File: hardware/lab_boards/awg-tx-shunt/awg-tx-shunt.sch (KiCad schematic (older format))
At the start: 20 parts, among them J1 1-1337543-0, J2 1-1337543-0, J3 1-1337543-0, J4 1-1337543-0, J5 1-1337543-0

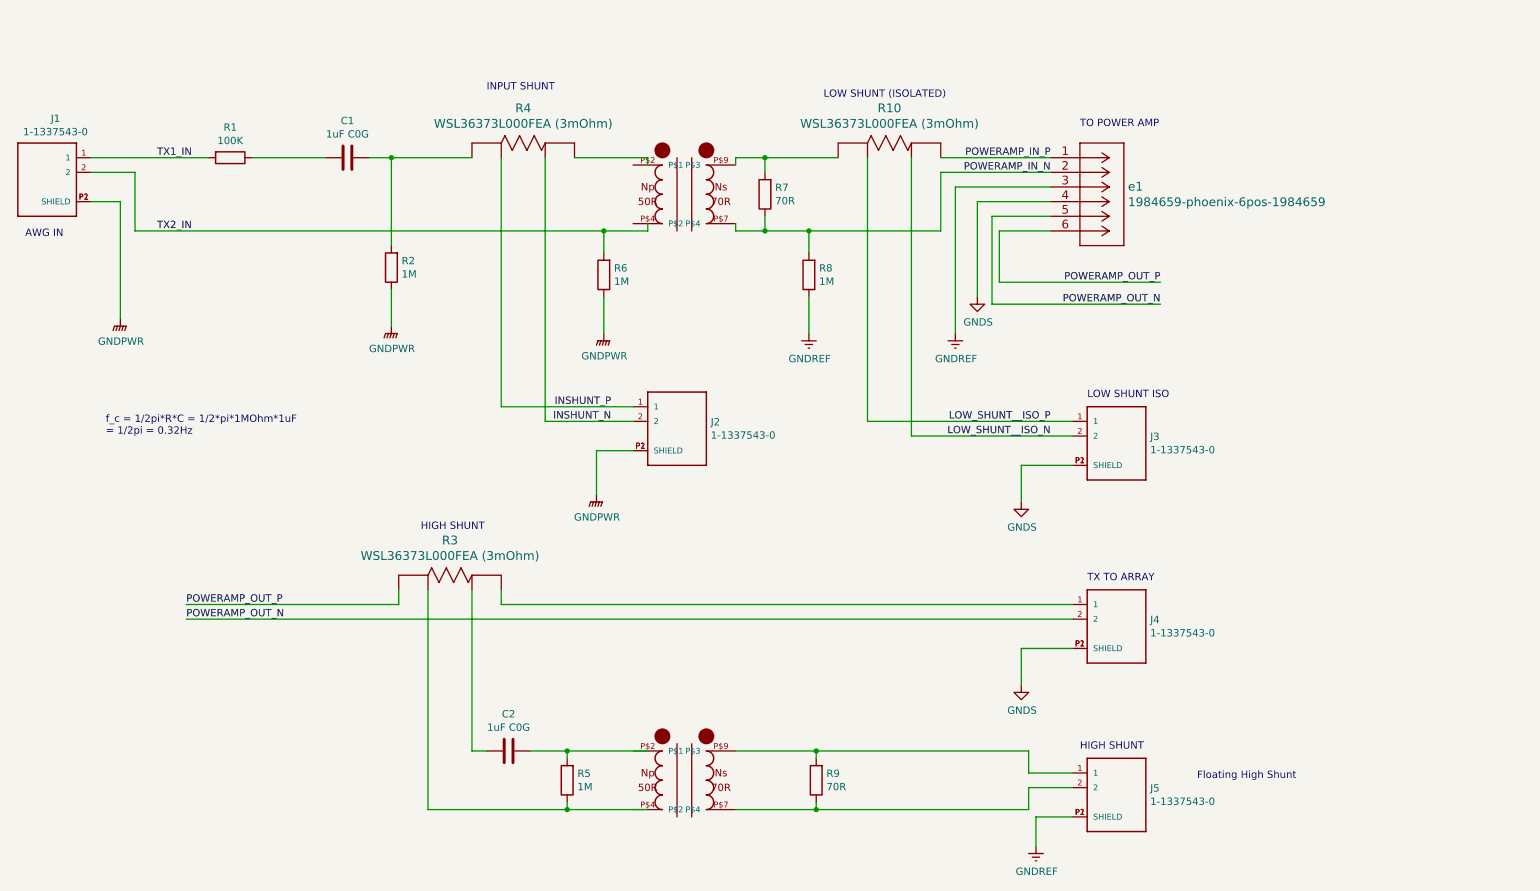
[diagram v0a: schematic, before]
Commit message: reworked the whole board so the grounds are properly isolated and can be connected to a common star ground offboard. No vias are necessary for routing, either, which is a good thing for signal integrity.
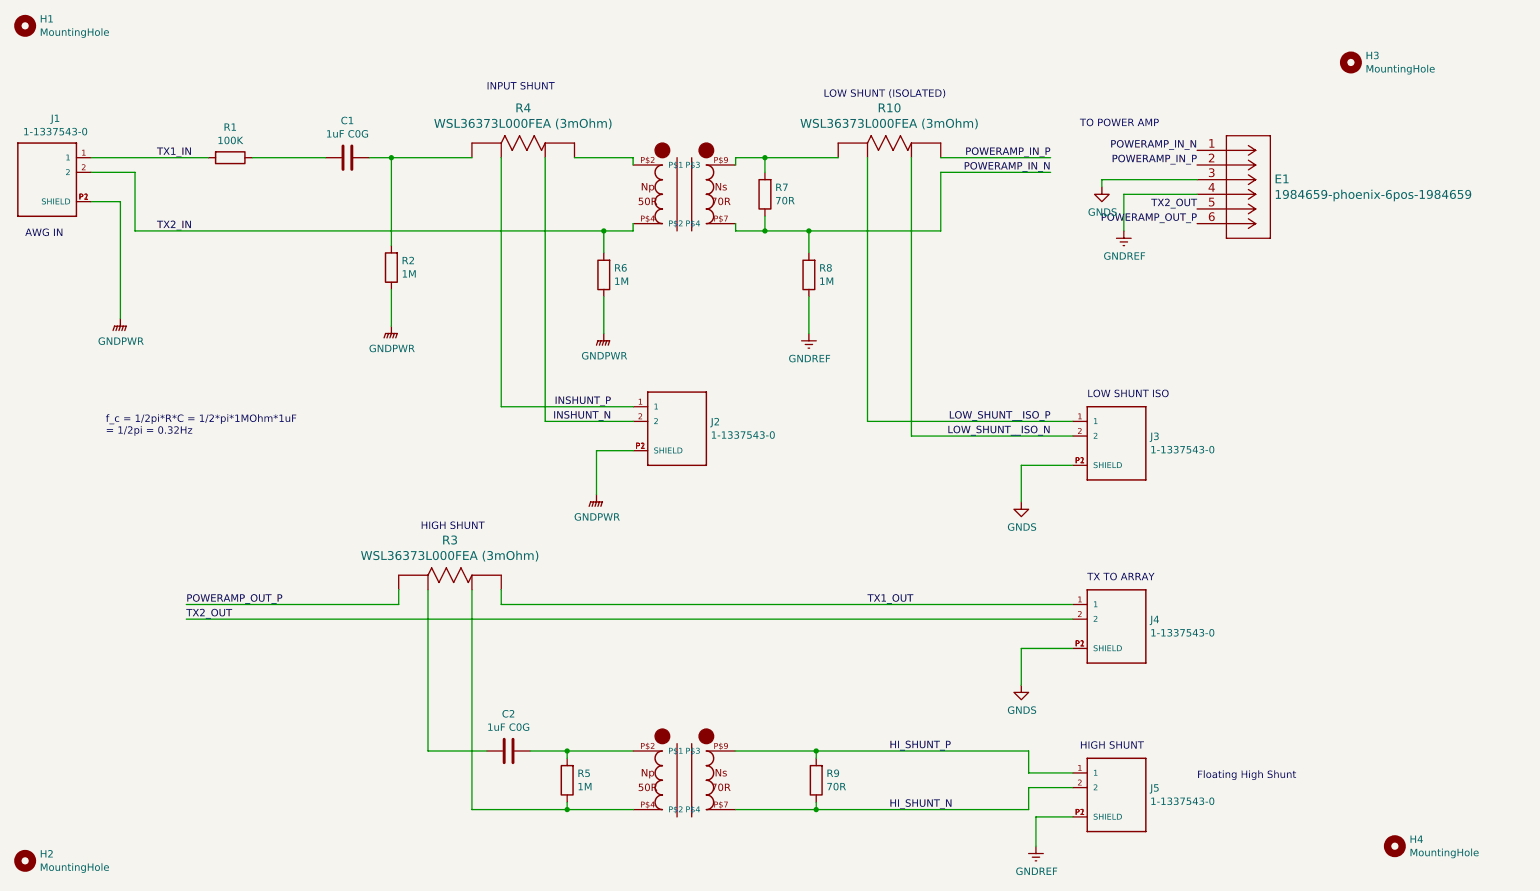
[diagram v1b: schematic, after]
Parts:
- added H1, H2, H3, H4: MountingHole, MountingHole:MountingHole_3.2mm_M3_Pad_Via, symbol Mechanical:MountingHole
- E1: renamed from e1; footprint CONN_1984659_PXC -> phoenix-6pos-1984659:1984659
- R10, R3, R4: footprint WSL3637_VIS -> WSL36373L000FEA:WSL36373L000FEA
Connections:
- net labels added: HI_SHUNT_N, HI_SHUNT_P, TX1_OUT, TX2_OUT
- net labels removed: POWERAMP_OUT_N
- wire segments 81 -> 75
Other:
- moved on the sheet: E1
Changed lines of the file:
@@
 F 0 "R4" H 4200 1988 60  0000 C CNN
 F 1 "WSL36373L000FEA (3mOhm)" H 4200 1882 60  0000 C CNN
-F 2 "WSL3637_VIS" H 4200 1315 60  0001 C CNN
+F 2 "WSL36373L000FEA:WSL36373L000FEA" H 4200 1315 60  0001 C CNN
 F 3 "" H 3950 1650 60  0000 C CNN
 	1    3950 1650
@@
 	3300 2550 3300 2800
 Wire Wire Line
-	4550 1650 5050 1650
-Wire Wire Line
-	5050 1650 5050 1700
-Wire Wire Line
-	5050 2100 5050 2150
+	4550 1650 4950 1650
 $Comp
 L Device:R R6
@@
 Wire Wire Line
 	4750 2300 4750 2150
-Connection ~ 4750 2150
-Wire Wire Line
-	4750 2150 5050 2150
 Wire Wire Line
 	4750 2600 4750 2850
@@
 F 0 "R3" H 3700 4938 60  0000 C CNN
 F 1 "WSL36373L000FEA (3mOhm)" H 3700 4832 60  0000 C CNN
-F 2 "WSL3637_VIS" H 3700 4265 60  0001 C CNN
+F 2 "WSL36373L000FEA:WSL36373L000FEA" H 3700 4265 60  0001 C CNN
 F 3 "" H 3450 4600 60  0000 C CNN
 	1    3450 4600
@@
 F 0 "R10" H 6700 1988 60  0000 C CNN
 F 1 "WSL36373L000FEA (3mOhm)" H 6700 1882 60  0000 C CNN
-F 2 "WSL3637_VIS" H 6700 1315 60  0001 C CNN
+F 2 "WSL36373L000FEA:WSL36373L000FEA" H 6700 1315 60  0001 C CNN
 F 3 "" H 6450 1650 60  0000 C CNN
 	1    6450 1650
@@
 	7050 1750 7050 2150
 Wire Wire Line
-	7800 1850 7150 1850
-Wire Wire Line
-	7800 1950 7300 1950
+	8800 1900 8300 1900
 Wire Wire Line
 	1250 1650 2050 1650
@@
 	1    0    0    -1
 $EndComp
-Wire Wire Line
-	7300 1950 7300 2600
-Wire Wire Line
-	7150 1850 7150 2850
 $Comp
 L Device:R R8
@@
 	4050 4700 7950 4700
 Wire Wire Line
-	3850 4600 3850 5700
-Wire Wire Line
-	3850 5700 3950 5700
-Wire Wire Line
-	5050 6100 4500 6100
-Wire Wire Line
-	3550 6100 3550 4600
-Wire Wire Line
 	1900 4800 7950 4800
 Wire Wire Line
@@
 TO POWER AMP
 $Comp
-L awg-tx-shunt-rescue:1984659-phoenix-6pos-1984659 e1
+L awg-tx-shunt-rescue:1984659-phoenix-6pos-1984659 E1
 U 1 1 5F8227D9
-P 7800 1650
-F 0 "e1" H 8328 1453 60  0000 L CNN
-F 1 "1984659-phoenix-6pos-1984659" H 8328 1347 60  0000 L CNN
-F 2 "CONN_1984659_PXC" H 8200 1390 60  0001 C CNN
-F 3 "" H 7800 1650 60  0000 C CNN
-	1    7800 1650
+P 8800 1600
+F 0 "E1" H 9328 1403 60  0000 L CNN
+F 1 "1984659-phoenix-6pos-1984659" H 9328 1297 60  0000 L CNN
+F 2 "phoenix-6pos-1984659:1984659" H 9200 1340 60  0001 C CNN
+F 3 "" H 8800 1600 60  0000 C CNN
+	1    8800 1600
 	1    0    0    -1
 $EndComp
@@
 Wire Wire Line
 	7600 3750 7600 4000
-Wire Wire Line
-	7800 2050 7400 2050
-Wire Wire Line
-	7400 2050 7400 2650
-Wire Wire Line
-	7400 2650 8550 2650
-Wire Wire Line
-	7800 2150 7450 2150
-Wire Wire Line
-	7450 2150 7450 2500
-Wire Wire Line
-	7450 2500 8550 2500
 $Comp
 L Conn-BNC-Amphenol-Isolated-1-1337543-0:1-1337543-0 J2
@@
 Wire Wire Line
 	6150 2150 7050 2150
-Text Label 8550 2500 2    50   ~ 0
-POWERAMP_OUT_P
-Text Label 8550 2650 2    50   ~ 0
-POWERAMP_OUT_N
 Wire Wire Line
 	4500 5700 4500 5750
-Connection ~ 4500 5700
-Wire Wire Line
-	4500 5700 5050 5700
 Wire Wire Line
 	4500 6050 4500 6100
-Connection ~ 4500 6100
-Wire Wire Line
-	4500 6100 3550 6100
+Wire Wire Line
+	4500 6100 3850 6100
 Wire Wire Line
 	7950 5000 7600 5000
@@
 Text Label 1900 4700 0    50   ~ 0
 POWERAMP_OUT_P
-Text Label 1900 4800 0    50   ~ 0
-POWERAMP_OUT_N
 Wire Wire Line
 	7950 6150 7700 6150
@@
 $EndComp
 $Comp
+L power:GNDREF #PWR0110
+U 1 1 5F8F2A85
+P 8300 2150
+F 0 "#PWR0110" H 8300 1900 50  0001 C CNN
+F 1 "GNDREF" H 8305 1977 50  0000 C CNN
+F 2 "" H 8300 2150 50  0001 C CNN
+F 3 "" H 8300 2150 50  0001 C CNN
+	1    8300 2150
+	1    0    0    -1
+$EndComp
+Text Label 6700 5700 0    50   ~ 0
+HI_SHUNT_P
+Text Label 6700 6100 0    50   ~ 0
+HI_SHUNT_N
+Text Label 6550 4700 0    50   ~ 0
+TX1_OUT
+Text Label 1900 4800 0    50   ~ 0
+TX2_OUT
+Wire Wire Line
+	4950 1650 4950 1700
+Wire Wire Line
+	4950 2100 4950 2150
+Wire Wire Line
+	4950 2150 4750 2150
+Connection ~ 4750 2150
+Wire Wire Line
+	4950 5700 4500 5700
+Connection ~ 4500 5700
+Wire Wire Line
+	4950 6100 4500 6100
+Connection ~ 4500 6100
+Wire Wire Line
+	3550 5700 3550 4600
+Wire Wire Line
+	3850 4600 3850 6100
+Wire Wire Line
+	3950 5700 3550 5700
+Text Label 8800 1600 2    50   ~ 0
+POWERAMP_IN_N
+Text Label 8800 1700 2    50   ~ 0
+POWERAMP_IN_P
+Text Label 8800 2100 2    50   ~ 0
+POWERAMP_OUT_P
+Text Label 8800 2000 2    50   ~ 0
+TX2_OUT
+$Comp
 L power:GNDS #PWR0109
 U 1 1 5F8EF65F
-P 7300 2600
-F 0 "#PWR0109" H 7300 2350 50  0001 C CNN
-F 1 "GNDS" H 7305 2427 50  0000 C CNN
-F 2 "" H 7300 2600 50  0001 C CNN
-F 3 "" H 7300 2600 50  0001 C CNN
-	1    7300 2600
-	1    0    0    -1
-$EndComp
-$Comp
-L power:GNDREF #PWR0110
-U 1 1 5F8F2A85
-P 7150 2850
-F 0 "#PWR0110" H 7150 2600 50  0001 C CNN
-F 1 "GNDREF" H 7155 2677 50  0000 C CNN
-F 2 "" H 7150 2850 50  0001 C CNN
-F 3 "" H 7150 2850 50  0001 C CNN
-	1    7150 2850
-	1    0    0    -1
-$EndComp
+P 8150 1850
+F 0 "#PWR0109" H 8150 1600 50  0001 C CNN
+F 1 "GNDS" H 8155 1677 50  0000 C CNN
+F 2 "" H 8150 1850 50  0001 C CNN
+F 3 "" H 8150 1850 50  0001 C CNN
+	1    8150 1850
+	1    0    0    -1
+$EndComp
+Wire Wire Line
+	8300 1900 8300 2150
+$Comp
+L Mechanical:MountingHole H3
+U 1 1 5F9CEF90
+P 9850 1000
+F 0 "H3" H 9950 1046 50  0000 L CNN
+F 1 "MountingHole" H 9950 955 50  0000 L CNN
+F 2 "MountingHole:MountingHole_3.2mm_M3_Pad_Via" H 9850 1000 50  0001 C CNN
+F 3 "~" H 9850 1000 50  0001 C CNN
+	1    9850 1000
+	1    0    0    -1
+$EndComp
+$Comp
+L Mechanical:MountingHole H4
+U 1 1 5F9CF560
+P 10150 6350
+F 0 "H4" H 10250 6396 50  0000 L CNN
+F 1 "MountingHole" H 10250 6305 50  0000 L CNN
+F 2 "MountingHole:MountingHole_3.2mm_M3_Pad_Via" H 10150 6350 50  0001 C CNN
+F 3 "~" H 10150 6350 50  0001 C CNN
+	1    10150 6350
+	1    0    0    -1
+$EndComp
+$Comp
+L Mechanical:MountingHole H2
+U 1 1 5F9D0AA7
+P 800 6450
+F 0 "H2" H 900 6496 50  0000 L CNN
+F 1 "MountingHole" H 900 6405 50  0000 L CNN
+F 2 "MountingHole:MountingHole_3.2mm_M3_Pad_Via" H 800 6450 50  0001 C CNN
+F 3 "~" H 800 6450 50  0001 C CNN
+	1    800  6450
+	1    0    0    -1
+$EndComp
+$Comp
+L Mechanical:MountingHole H1
+U 1 1 5F9D154E
+P 800 750
+F 0 "H1" H 900 796 50  0000 L CNN
+F 1 "MountingHole" H 900 705 50  0000 L CNN
+F 2 "MountingHole:MountingHole_3.2mm_M3_Pad_Via" H 800 750 50  0001 C CNN
+F 3 "~" H 800 750 50  0001 C CNN
+	1    800  750
+	1    0    0    -1
+$EndComp
+Wire Wire Line
+	8800 1800 8150 1800
+Wire Wire Line
+	8150 1800 8150 1850
 $EndSCHEMATC
